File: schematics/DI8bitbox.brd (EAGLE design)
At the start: 72.1 x 41.9 mm, 20 parts, among them Q1 500mA/300V, X1 332-02, X2 332-02

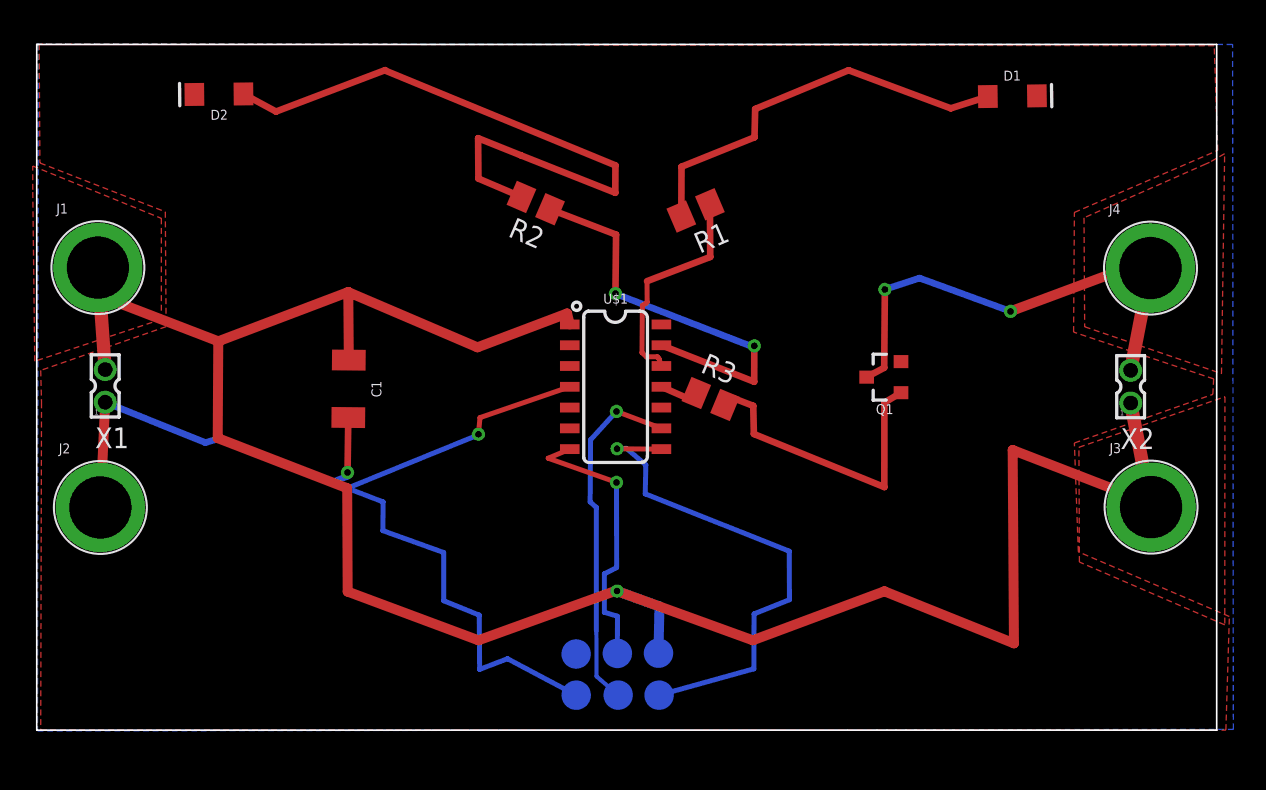
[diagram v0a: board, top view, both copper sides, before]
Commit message: ordered rev.b at safepcb and mouser BOM updated
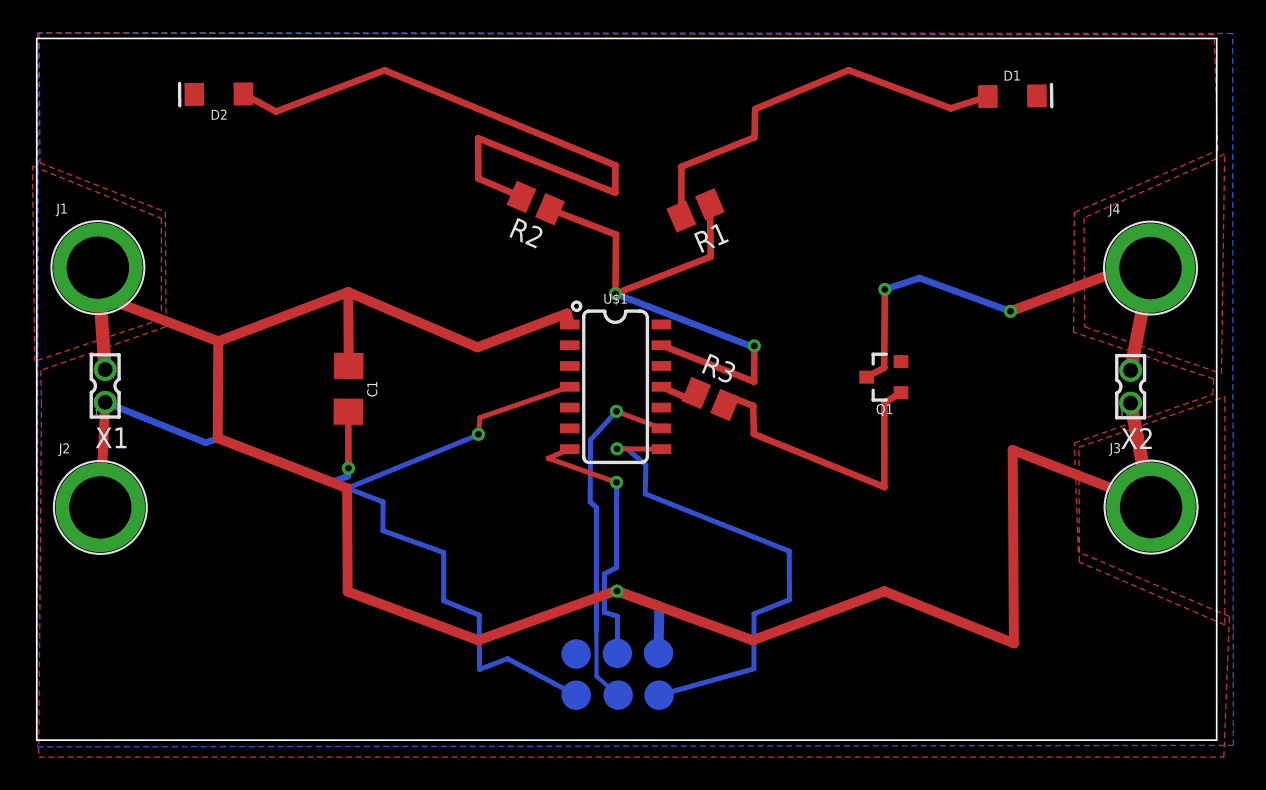
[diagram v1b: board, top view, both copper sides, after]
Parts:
- C1: value 10uF -> 100nF; device SparkFun-Capacitors:1210 -> SparkFun-Capacitors:1206
- R1, R2: value 220r -> 100r
- R3: value 220r -> 1k
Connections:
- removed net N$4: R1.1, U$1.12
- net N$1: now also R1.1
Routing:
- net N$4: track 13.5 -> 0.00 mm
- net N$1: track 25.8 -> 35.3 mm
- net VCC: track 144.9 -> 145.6 mm
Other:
- board size 72.1 x 41.9 mm -> 72.1 x 42.9 mm
